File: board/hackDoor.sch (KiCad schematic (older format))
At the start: 9 parts

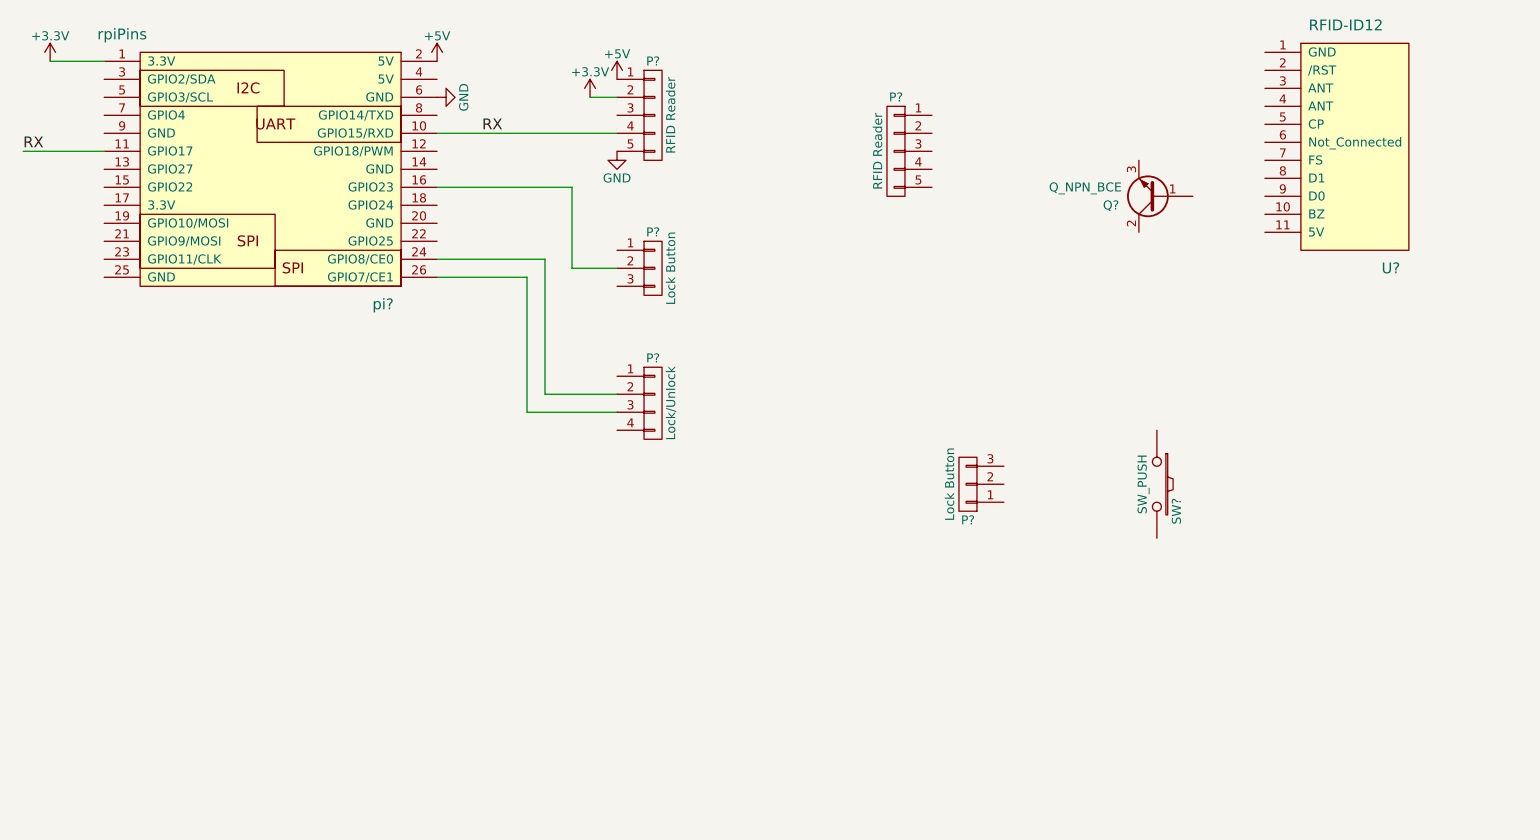
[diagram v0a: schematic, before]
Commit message: added secondary schematics. added netlist and footprint association. started pcb layout.
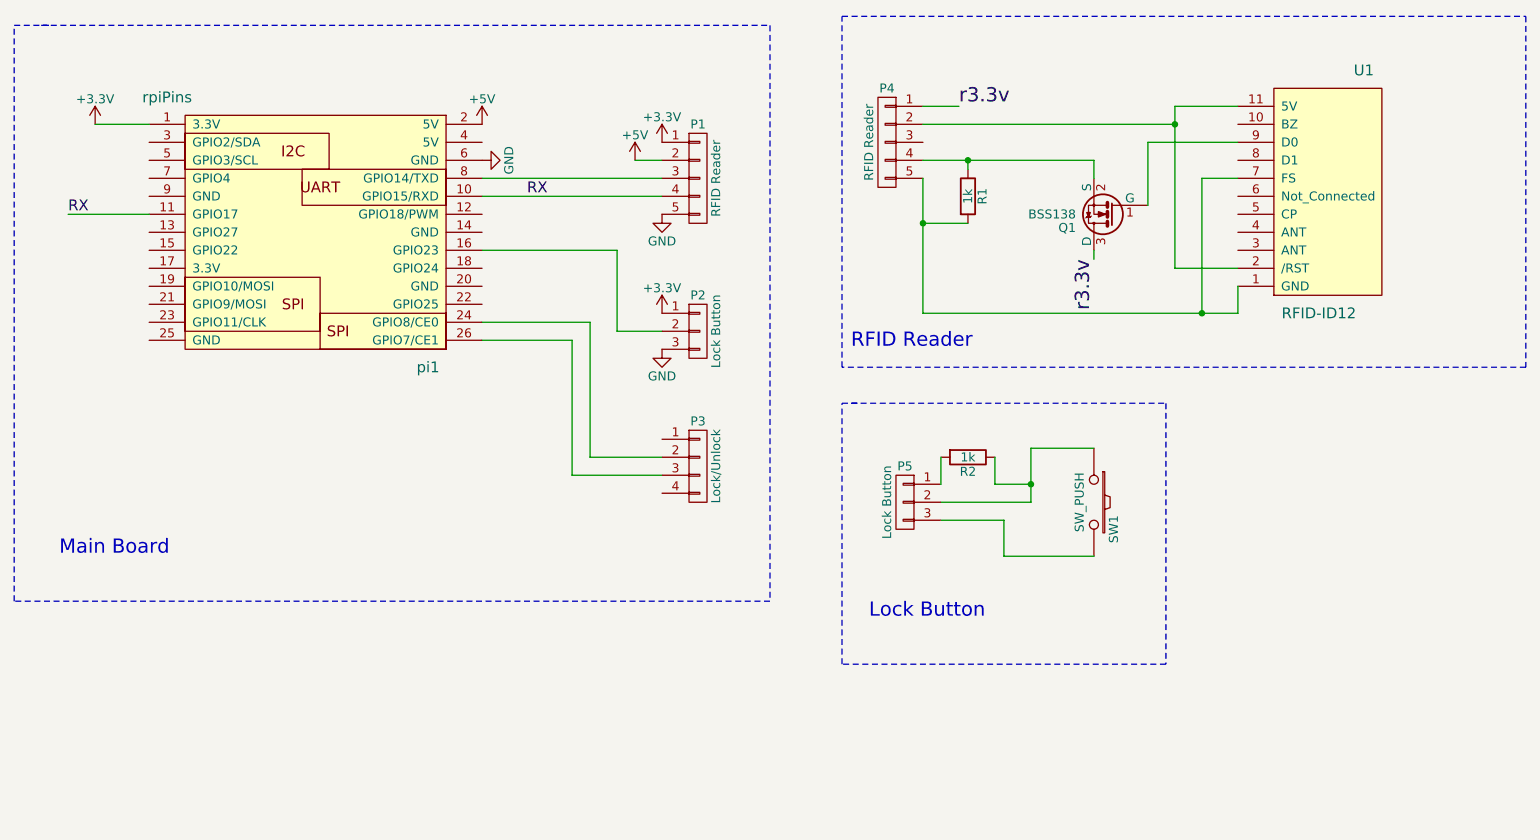
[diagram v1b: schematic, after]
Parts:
- removed Q?: Q_NPN_BCE, symbol Q_NPN_BCE
- removed pi?: rpiPins, symbol rpiPins
- added Q1: BSS138, TO_SOT_Packages_SMD:SOT-23, symbol BSS138
- added R1, R2: 1k, Resistors_SMD:R_0805_HandSoldering, symbol R
- added pi1: rpiPins, Pin_Headers:Pin_Header_Straight_2x13, symbol rpiPins
- P1, P4: renamed from P?; footprint (none) -> Pin_Headers:Pin_Header_Angled_1x05
- P2, P5: renamed from P?; footprint (none) -> Pin_Headers:Pin_Header_Angled_1x03
- P3: renamed from P?; footprint (none) -> Pin_Headers:Pin_Header_Angled_1x04
- gave numbers to parts that had none: 2
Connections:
- net +3V3: now also P1.1 (P1), P2.1 (P1), pi1.1 (3.3V); no longer P1.2 (P2)
- net +5V: now also P1.2 (P2), pi1.2 (5V); no longer P1.1 (P1)
- net GND: now also P2.3 (P3), pi1.6 (GND)
- net RX: now also pi1.10 (GPIO15/RXD), pi1.11 (GPIO17)
- net at P2.2 (P2): now also pi1.16 (GPIO23)
- net at P3.2 (P2): now also pi1.24 (GPIO8/CE0)
- net at P3.3 (P3): now also pi1.26 (GPIO7/CE1)
- net at P1.3 (P3): now also pi1.8 (GPIO14/TXD)
- net at SW1.1: now also P5.2 (P2), R2.1
- net at SW1.2: now also P5.3 (P3)
- net at P5.1 (P1): now also R2.2
- net r3.3v: now reaches P4.1 (P1)
- net r3.3v: now also Q1.3 (D)
- net at P4.2 (P2): now also U1.11 (5V), U1.2 (/RST)
- net at P4.4 (P4): now also Q1.2 (S), R1.1
- net at P4.5 (P5): now also U1.1 (GND), U1.7 (FS), R1.2
- net at U1.9 (D0): now also Q1.1 (G)
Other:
- note added: "Lock Button"
- note added: "Main Board\n"
- note added: "RFID Reader"
- moved on the sheet: P1, P2, P3, P4, P5, SW1, U1

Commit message: finished preliminary board routing. added rfid reader footprint
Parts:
- SW1: footprint (none) -> Buttons_Switches_ThroughHole:SW_PUSH
- U1: footprint (none) -> hackDoor:rfid-id12
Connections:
- net +3V3: now also P3.1 (P1)
- net GND: now also P3.4 (P4)
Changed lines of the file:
@@
 LIBS:contrib
 LIBS:valves
-LIBS:fm_tuner
 LIBS:hackDoor
 LIBS:hackDoor-cache
@@
 F 0 "SW1" H 6800 3460 50  0000 C CNN
 F 1 "SW_PUSH" H 6650 3270 50  0000 C CNN
-F 2 "" H 6650 3350 50  0001 C CNN
+F 2 "Buttons_Switches_ThroughHole:SW_PUSH" H 6650 3350 50  0001 C CNN
 F 3 "" H 6650 3350 50  0000 C CNN
 	1    6650 3350
@@
 F 0 "U1" H 8150 950 60  0000 C CNN
 F 1 "RFID-ID12" H 7900 2300 60  0000 C CNN
-F 2 "" H 7350 2400 60  0001 C CNN
+F 2 "hackDoor:rfid-id12" H 7350 2400 60  0001 C CNN
 F 3 "" H 7350 2400 60  0001 C CNN
 	1    7350 2400
@@
 Wire Wire Line
 	7100 1150 7100 2050
+$Comp
+L +3.3V #PWR09
+U 1 1 5812A101
+P 4250 3000
+F 0 "#PWR09" H 4250 2850 50  0001 C CNN
+F 1 "+3.3V" H 4250 3140 50  0000 C CNN
+F 2 "" H 4250 3000 50  0000 C CNN
+F 3 "" H 4250 3000 50  0000 C CNN
+	1    4250 3000
+	1    0    0    -1
+$EndComp
+$Comp
+L GND #PWR010
+U 1 1 5812A12B
+P 4250 3300
+F 0 "#PWR010" H 4250 3050 50  0001 C CNN
+F 1 "GND" H 4250 3150 50  0000 C CNN
+F 2 "" H 4250 3300 50  0000 C CNN
+F 3 "" H 4250 3300 50  0000 C CNN
+	1    4250 3300
+	1    0    0    -1
+$EndComp
 $EndSCHEMATC

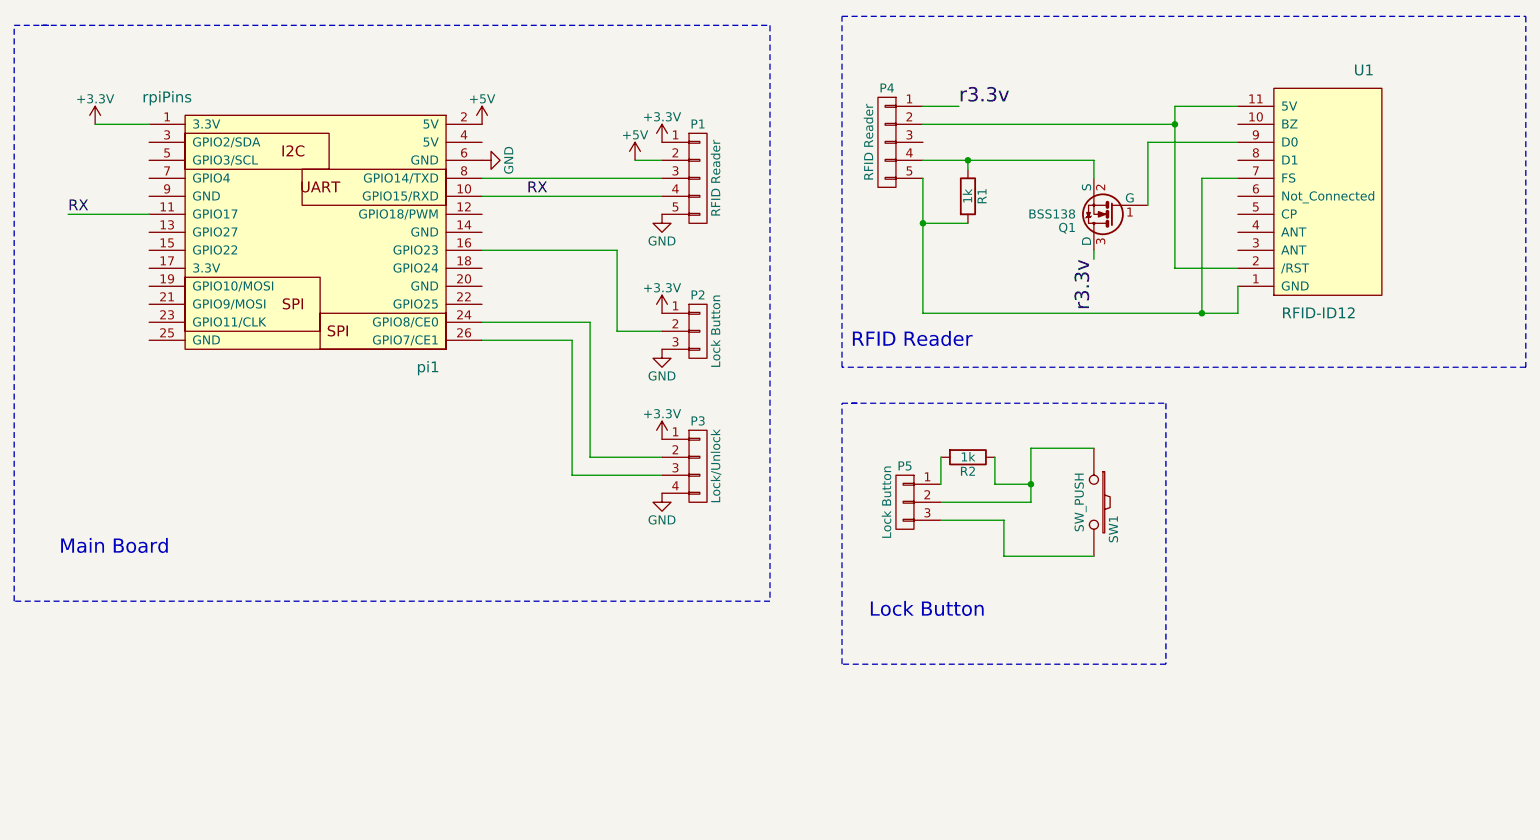
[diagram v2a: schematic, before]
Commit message: added door and lock sensors. fixed the logic converter circuit on the rfid board
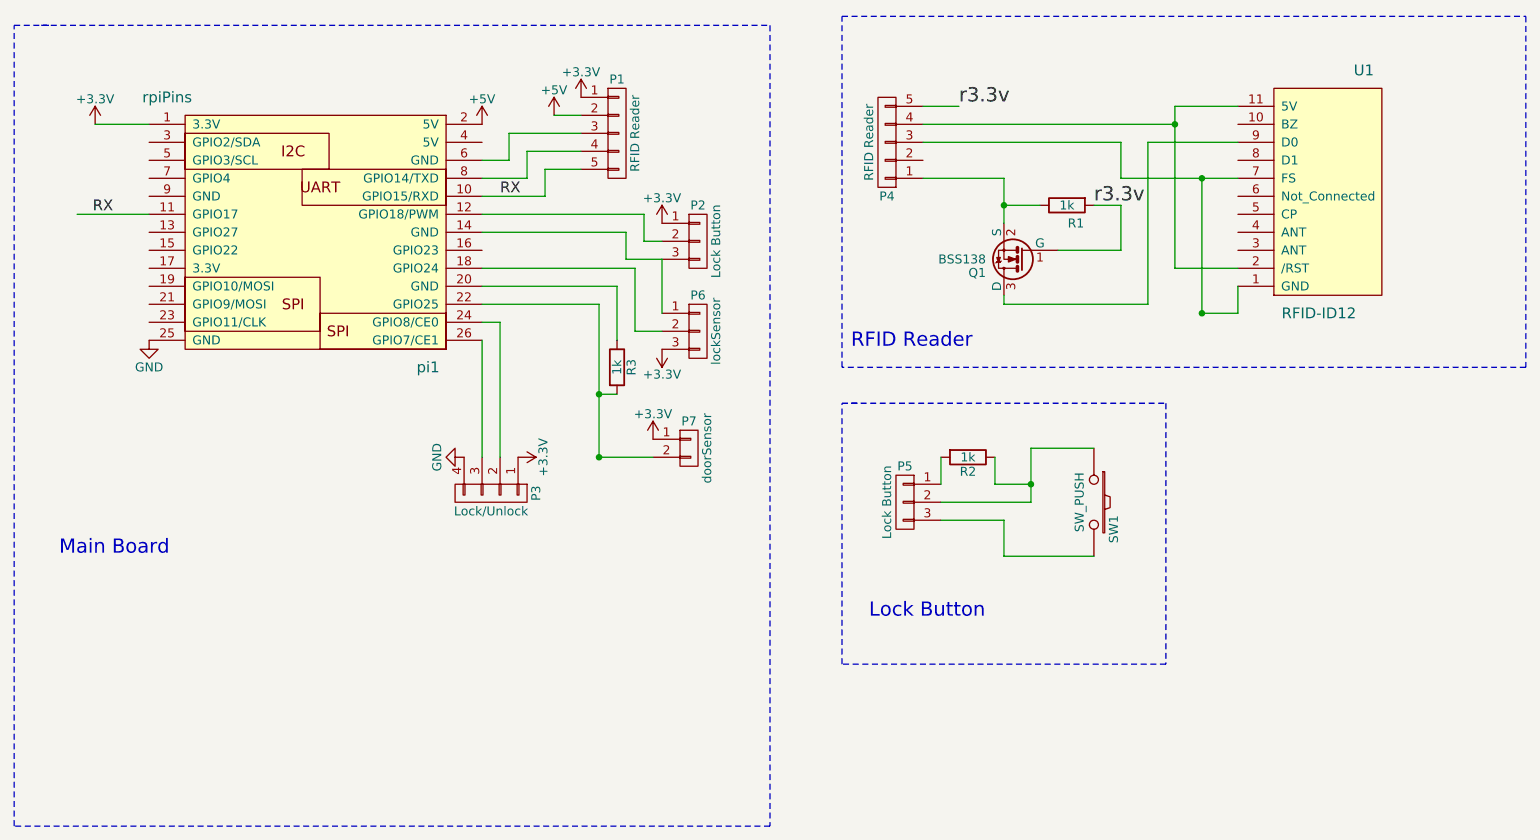
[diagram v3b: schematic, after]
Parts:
- added P6: lockSensor, Pin_Headers:Pin_Header_Angled_1x03, symbol CONN_01X03
- added P7: doorSensor, Pin_Headers:Pin_Header_Angled_1x02, symbol CONN_01X02
- added R3: 1k, Resistors_SMD:R_0805_HandSoldering, symbol R
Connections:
- net +3V3: now also P6.3 (P3), P7.1 (P1)
- net GND: now also pi1.25 (GND); no longer P1.5 (P5), P2.3 (P3), pi1.6 (GND)
- net RX: now also P1.5 (P5); no longer P1.4 (P4)
- net r3.3v: now also P4.5 (P5), Q1.1 (G), R1.2; no longer P4.1 (P1), Q1.3 (D)
- net at P1.3 (P3): now also pi1.6 (GND); no longer pi1.8 (GPIO14/TXD)
- net at P2.2 (P2): now also pi1.12 (GPIO18/PWM); no longer pi1.16 (GPIO23)
- net at U1.11 (5V), U1.2 (/RST): now also P4.4 (P4); no longer P4.2 (P2)
- net at P4.3 (P3): now also U1.1 (GND), U1.7 (FS)
- net at Q1.2 (S), R1.1: now also P4.1 (P1); no longer P4.4 (P4)
- net at U1.9 (D0): now also Q1.3 (D); no longer Q1.1 (G)
- net at pi1.14 (GND): now also P2.3 (P3), P6.1 (P1)
- net at pi1.18 (GPIO24): now also P6.2 (P2)
- net at pi1.20 (GND): now also R3.1
- net at pi1.22 (GPIO25): now also P7.2 (P2), R3.2
- new net: P1.4 (P4), pi1.8 (GPIO14/TXD)
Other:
- moved on the sheet: P1, P2, P3, Q1, R1
